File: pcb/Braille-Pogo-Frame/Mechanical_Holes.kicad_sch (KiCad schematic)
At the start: 16 parts

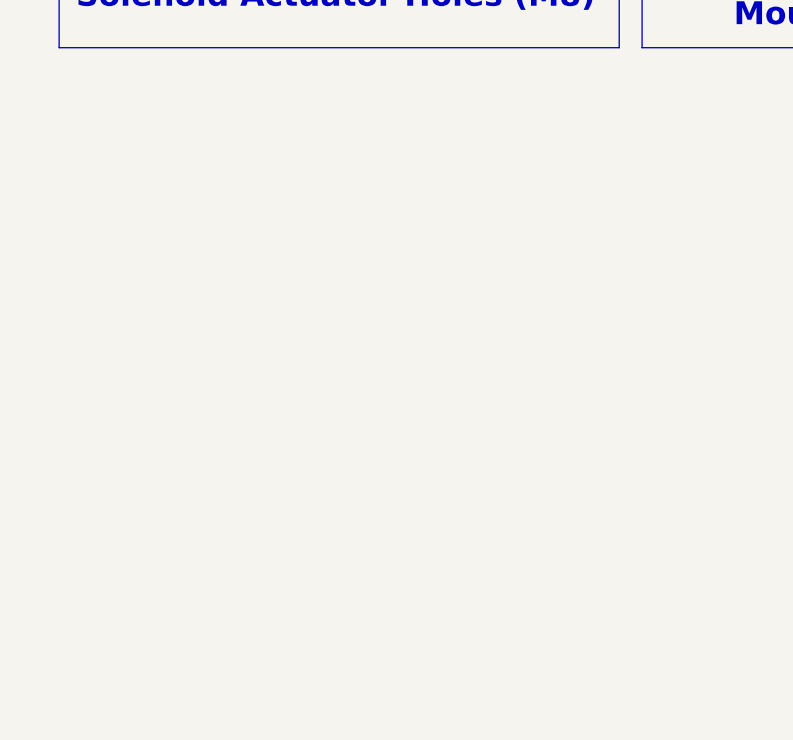
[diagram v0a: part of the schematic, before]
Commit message: PCB: Place motor drivers and horiz. rail mounts
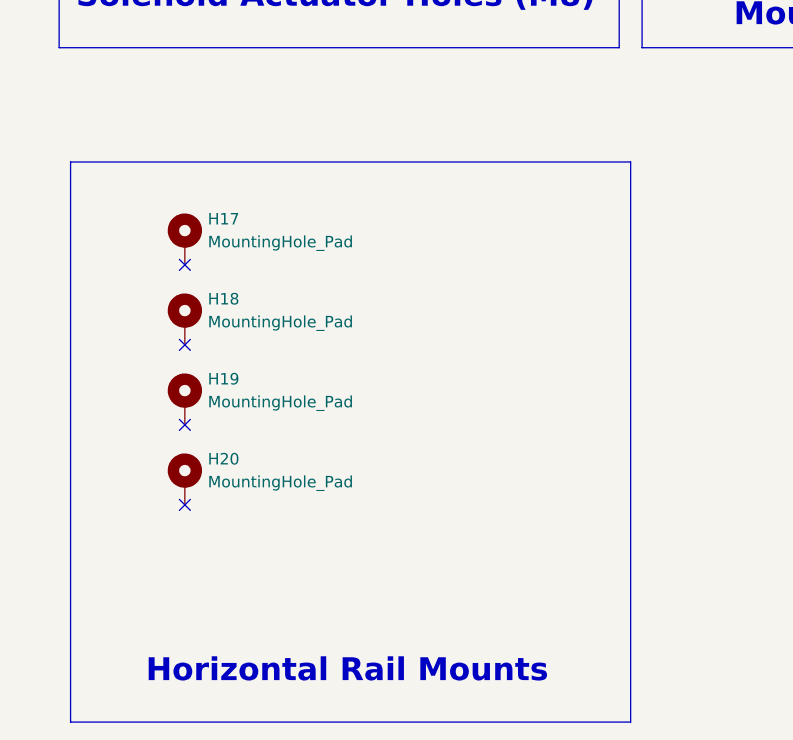
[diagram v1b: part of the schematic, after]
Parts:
- added H17, H18, H19, H20: MountingHole_Pad, 00-lib-footprints:HorizMounting_4x_M2_and_M3_Middle, symbol Mechanical:MountingHole_Pad
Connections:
- no-connect marks 16 -> 20
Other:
- note added: "Horizontal Rail Mounts"
